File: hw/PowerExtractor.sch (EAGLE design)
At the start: 86 parts, among them IC1 LM358D, Q1 IRL530N, Q2 BSS84, Q3 BC847SMD, Q4 IRF7416, Q5 IRL530N, Q6 IRL530N, T1 BCV47, T2 BCV47, T3 BCV47, U1 ZXCT1086E5TA, U2 ZXCT1086E5TA, X4 LDD700L

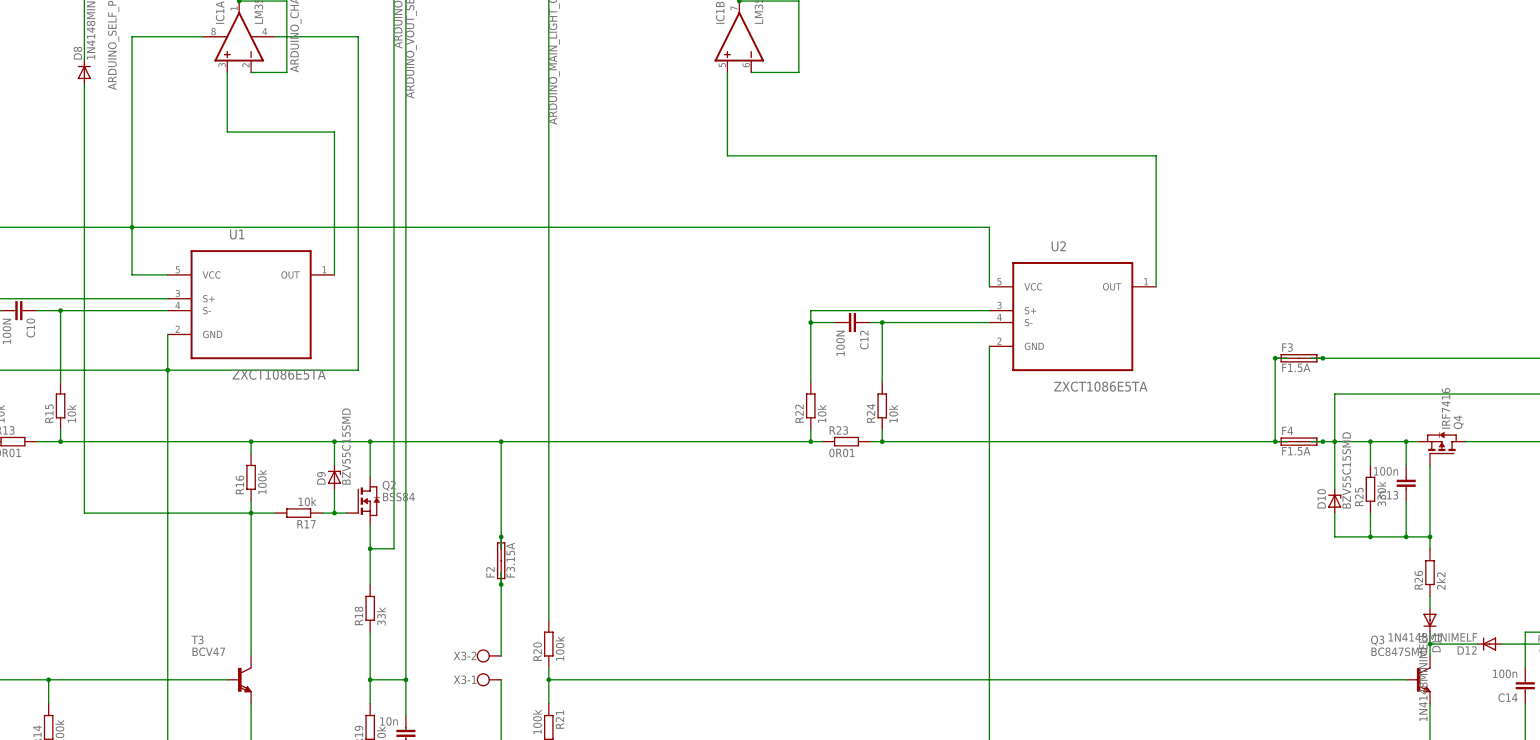
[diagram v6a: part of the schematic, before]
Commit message: Fixed BSS84 pinout
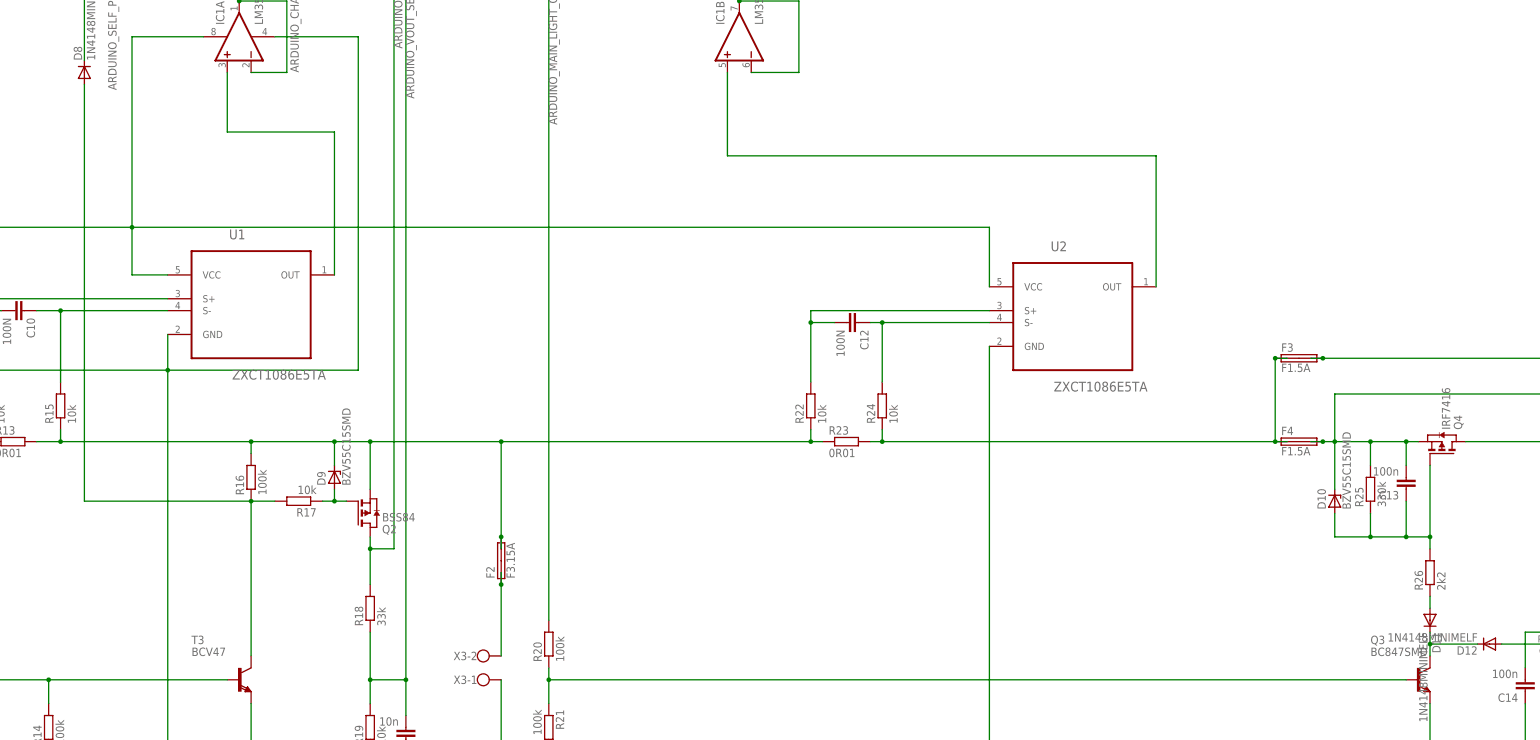
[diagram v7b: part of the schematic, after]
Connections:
- net ARDUINO_VIN: now also Q2.D; no longer Q2.S
- net BAT+FUSED: now also Q2.S; no longer Q2.D
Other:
- moved on the sheet: R17
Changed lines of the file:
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@@
 <part name="F2" library="fuse" deviceset="SHK20L" device="" value="F3.15A"/>
 <part name="F1" library="fuse" deviceset="SHK20L" device="" value="F3.15A"/>
-<part name="Q2" library="triakcz" deviceset="BSS84" device=""/>
 <part name="R14" library="rcl" deviceset="R-EU_" device="M0805" value="100k"/>
 <part name="X3" library="con-wago-500" deviceset="W237-102" device=""/>
@@
 <part name="D8" library="triakcz" deviceset="1N4148" device="MINIMELF" value="1N4148MINIMELF"/>
 <part name="D4" library="triakcz" deviceset="1N4148" device="MINIMELF"/>
+<part name="Q2" library="triakcz" deviceset="BSS84" device=""/>
 </parts>
 <sheets>
@@
 <instance part="C9" gate="G$1" x="175.26" y="35.56"/>
 <instance part="R16" gate="G$1" x="248.92" y="78.74" rot="R90"/>
-<instance part="R17" gate="G$1" x="259.08" y="71.12" rot="R180"/>
+<instance part="R17" gate="G$1" x="259.08" y="73.66" rot="R180"/>
 <instance part="D9" gate="G$1" x="266.7" y="78.74" rot="R90"/>
 <instance part="F2" gate="G$1" x="302.26" y="60.96" rot="R90"/>
 <instance part="F1" gate="G$1" x="-83.82" y="50.8"/>
-<instance part="Q2" gate="Q" x="274.32" y="73.66"/>
 <instance part="R14" gate="G$1" x="205.74" y="25.4" rot="R90"/>
 <instance part="X3" gate="-1" x="297.18" y="35.56"/>
@@
 <instance part="R13" gate="G$1" x="198.12" y="86.36"/>
 <instance part="U1" gate="A" x="248.92" y="119.38"/>
-<instance part="Q4" gate="A" x="502.92" y="86.36" rot="MR90"/>
+<instance part="Q4" gate="A" x="502.92" y="86.36" rot="R90"/>
 <instance part="Q3" gate="G$1" x="497.84" y="35.56"/>
 <instance part="R20" gate="G$1" x="312.42" y="43.18" rot="R90"/>
@@
 <instance part="D8" gate="G$1" x="213.36" y="165.1" rot="R90"/>
 <instance part="D4" gate="G$1" x="116.84" y="259.08" rot="R90"/>
+<instance part="Q2" gate="G$1" x="274.32" y="71.12"/>
 </instances>
 <busses>
@@
 <segment>
 <pinref part="R18" gate="G$1" pin="2"/>
-<wire x1="274.32" y1="68.58" x2="274.32" y2="63.5" width="0.1524" layer="91"/>
-<pinref part="Q2" gate="Q" pin="S"/>
 <wire x1="274.32" y1="63.5" x2="274.32" y2="55.88" width="0.1524" layer="91"/>
 <wire x1="274.32" y1="63.5" x2="279.4" y2="63.5" width="0.1524" layer="91"/>
-<junction x="274.32" y="63.5"/>
 <wire x1="279.4" y1="63.5" x2="279.4" y2="243.84" width="0.1524" layer="91"/>
 <label x="279.4" y="185.42" size="1.778" layer="95" rot="R270"/>
@@
 <wire x1="40.64" y1="226.06" x2="58.42" y2="226.06" width="0.1524" layer="91"/>
 <junction x="58.42" y="226.06"/>
+<pinref part="Q2" gate="G$1" pin="D"/>
+<wire x1="274.32" y1="66.04" x2="274.32" y2="63.5" width="0.1524" layer="91"/>
+<junction x="274.32" y="63.5"/>
 </segment>
 </net>
@@
 <pinref part="D9" gate="G$1" pin="A"/>
 <pinref part="R17" gate="G$1" pin="1"/>
-<wire x1="269.24" y1="71.12" x2="266.7" y2="71.12" width="0.1524" layer="91"/>
-<pinref part="Q2" gate="Q" pin="G"/>
-<wire x1="266.7" y1="71.12" x2="264.16" y2="71.12" width="0.1524" layer="91"/>
-<wire x1="266.7" y1="76.2" x2="266.7" y2="71.12" width="0.1524" layer="91"/>
-<junction x="266.7" y="71.12"/>
+<wire x1="269.24" y1="73.66" x2="266.7" y2="73.66" width="0.1524" layer="91"/>
+<wire x1="266.7" y1="73.66" x2="264.16" y2="73.66" width="0.1524" layer="91"/>
+<wire x1="266.7" y1="76.2" x2="266.7" y2="73.66" width="0.1524" layer="91"/>
+<junction x="266.7" y="73.66"/>
+<pinref part="Q2" gate="G$1" pin="G"/>
 </segment>
 </net>
@@
 <net name="BAT+FUSED" class="0">
 <segment>
-<pinref part="Q2" gate="Q" pin="D"/>
-<wire x1="274.32" y1="78.74" x2="274.32" y2="86.36" width="0.1524" layer="91"/>
 <pinref part="F2" gate="G$1" pin="2B"/>
 <pinref part="F2" gate="G$1" pin="2A"/>
@@
 <wire x1="302.26" y1="66.04" x2="302.26" y2="86.36" width="0.1524" layer="91"/>
 <wire x1="302.26" y1="86.36" x2="274.32" y2="86.36" width="0.1524" layer="91"/>
-<junction x="274.32" y="86.36"/>
+<pinref part="D9" gate="G$1" pin="C"/>
 <wire x1="274.32" y1="86.36" x2="266.7" y2="86.36" width="0.1524" layer="91"/>
-<pinref part="D9" gate="G$1" pin="C"/>
 <wire x1="266.7" y1="81.28" x2="266.7" y2="86.36" width="0.1524" layer="91"/>
 <junction x="266.7" y="86.36"/>
@@
 <wire x1="368.3" y1="86.36" x2="370.84" y2="86.36" width="0.1524" layer="91"/>
 <wire x1="368.3" y1="88.9" x2="368.3" y2="86.36" width="0.1524" layer="91"/>
+<pinref part="Q2" gate="G$1" pin="S"/>
+<wire x1="274.32" y1="76.2" x2="274.32" y2="86.36" width="0.1524" layer="91"/>
+<junction x="274.32" y="86.36"/>
 </segment>
 </net>
@@
 <pinref part="R16" gate="G$1" pin="1"/>
 <pinref part="R17" gate="G$1" pin="2"/>
-<wire x1="254" y1="71.12" x2="248.92" y2="71.12" width="0.1524" layer="91"/>
-<wire x1="248.92" y1="71.12" x2="248.92" y2="73.66" width="0.1524" layer="91"/>
-<junction x="248.92" y="71.12"/>
+<wire x1="254" y1="73.66" x2="248.92" y2="73.66" width="0.1524" layer="91"/>
+<junction x="248.92" y="73.66"/>
 <pinref part="T3" gate="G$1" pin="C"/>
-<wire x1="248.92" y1="71.12" x2="248.92" y2="40.64" width="0.1524" layer="91"/>
+<wire x1="248.92" y1="73.66" x2="248.92" y2="40.64" width="0.1524" layer="91"/>
 <pinref part="D8" gate="G$1" pin="A"/>
-<wire x1="213.36" y1="162.56" x2="213.36" y2="71.12" width="0.1524" layer="91"/>
-<wire x1="213.36" y1="71.12" x2="248.92" y2="71.12" width="0.1524" layer="91"/>
-</segment>
-</net>
+<wire x1="213.36" y1="162.56" x2="213.36" y2="73.66" width="0.1524" layer="91"/>
+<wire x1="213.36" y1="73.66" x2="248.92" y2="73.66" width="0.1524" layer="91"/>
+</segment>
+</net>

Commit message: Fixing various bugs
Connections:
- net ARDUINO_VIN_ANALOG renamed ARDUINO_VIN_SENSE
- net N$11 renamed ARDUINO_IOUT_SENSE
- net N$34 renamed DISPLAY_SDA
- net N$35 renamed DISPLAY_SCL
- net +5V: now also DSPL.2; no longer DSPL.1
- net GND: now also DSPL.1; no longer DSPL.2
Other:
- note added: "GND VCC SCL SDA"
- note removed: "VCC GND SCL SDA"
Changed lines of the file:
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@@
 <plain>
 <text x="137.16" y="180.34" size="1.778" layer="91" rot="R90">D2/D3 ONLY !</text>
-<text x="129.54" y="289.56" size="1.778" layer="91">VCC GND SCL SDA</text>
+<text x="129.54" y="289.56" size="1.778" layer="91">GND VCC SCL SDA</text>
 </plain>
 <instances>
@@
 </segment>
 </net>
-<net name="ARDUINO_VIN_ANALOG" class="0">
+<net name="ARDUINO_VIN_SENSE" class="0">
 <segment>
 <pinref part="R9" gate="G$1" pin="2"/>
@@
 <wire x1="27.94" y1="264.16" x2="68.58" y2="264.16" width="0.1524" layer="91"/>
 <wire x1="68.58" y1="264.16" x2="68.58" y2="284.48" width="0.1524" layer="91"/>
-<pinref part="DSPL" gate="A" pin="2"/>
-<wire x1="139.7" y1="284.48" x2="139.7" y2="264.16" width="0.1524" layer="91"/>
-<wire x1="139.7" y1="264.16" x2="68.58" y2="264.16" width="0.1524" layer="91"/>
+<wire x1="137.16" y1="264.16" x2="68.58" y2="264.16" width="0.1524" layer="91"/>
 <junction x="68.58" y="264.16"/>
 <wire x1="27.94" y1="200.66" x2="27.94" y2="20.32" width="0.1524" layer="91"/>
@@
 <wire x1="248.92" y1="30.48" x2="248.92" y2="20.32" width="0.1524" layer="91"/>
 <junction x="248.92" y="20.32"/>
+<pinref part="DSPL" gate="A" pin="1"/>
+<wire x1="137.16" y1="284.48" x2="137.16" y2="264.16" width="0.1524" layer="91"/>
 </segment>
 </net>
@@
 </segment>
 </net>
-<net name="N$34" class="0">
+<net name="DISPLAY_SDA" class="0">
 <segment>
 <wire x1="73.66" y1="198.12" x2="53.34" y2="198.12" width="0.1524" layer="91"/>
@@
 </segment>
 </net>
-<net name="N$35" class="0">
+<net name="DISPLAY_SCL" class="0">
 <segment>
 <pinref part="DSPL" gate="A" pin="3"/>
@@
 </segment>
 </net>
-<net name="N$11" class="0">
+<net name="ARDUINO_IOUT_SENSE" class="0">
 <segment>
 <pinref part="IC1" gate="B" pin="-IN"/>
@@
 <wire x1="48.26" y1="193.04" x2="73.66" y2="193.04" width="0.1524" layer="91"/>
 <pinref part="A1" gate="G$1" pin="A6"/>
+<label x="355.6" y="220.98" size="1.778" layer="95" rot="R90"/>
 </segment>
 </net>
@@
 <junction x="-40.64" y="220.98"/>
 <pinref part="A1" gate="G$1" pin="5V"/>
-<pinref part="DSPL" gate="A" pin="1"/>
-<wire x1="137.16" y1="284.48" x2="137.16" y2="246.38" width="0.1524" layer="91"/>
-<wire x1="137.16" y1="246.38" x2="55.88" y2="246.38" width="0.1524" layer="91"/>
+<wire x1="139.7" y1="246.38" x2="55.88" y2="246.38" width="0.1524" layer="91"/>
 <wire x1="55.88" y1="246.38" x2="55.88" y2="220.98" width="0.1524" layer="91"/>
 <junction x="55.88" y="220.98"/>
@@
 <wire x1="15.24" y1="114.3" x2="15.24" y2="132.08" width="0.1524" layer="91"/>
 <junction x="15.24" y="132.08"/>
-</segment>
-</net>
+<pinref part="DSPL" gate="A" pin="2"/>
+<wire x1="139.7" y1="246.38" x2="139.7" y2="284.48" width="0.1524" layer="91"/>
+</segment>
+</net>
